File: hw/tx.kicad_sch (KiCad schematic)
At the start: 40 parts, among them T301 BN-43-202_DualPri_CTSec, U301 ICE40UP5K-SG48ITR, Y301 40MHz

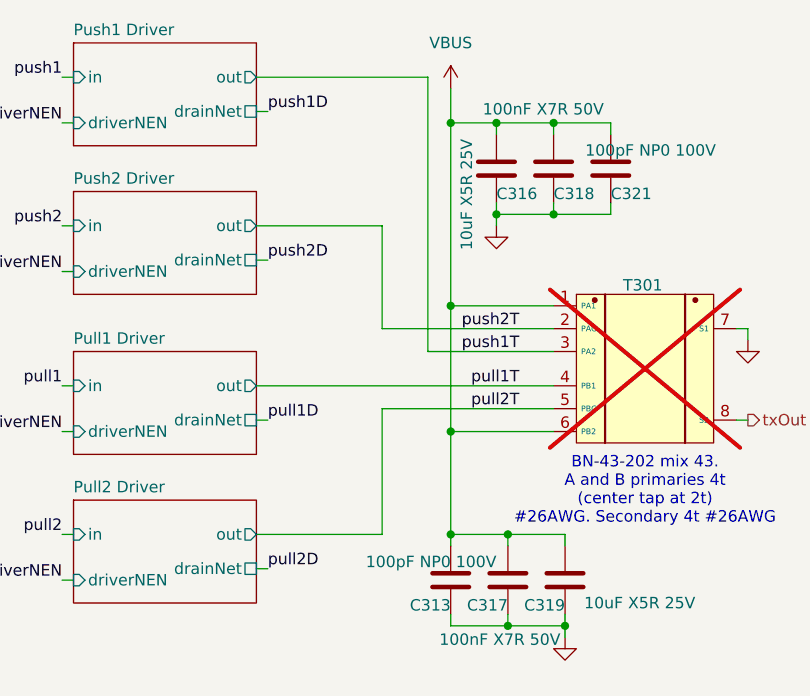
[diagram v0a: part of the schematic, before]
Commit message: Use relays and do layout over again to make these damned things fit
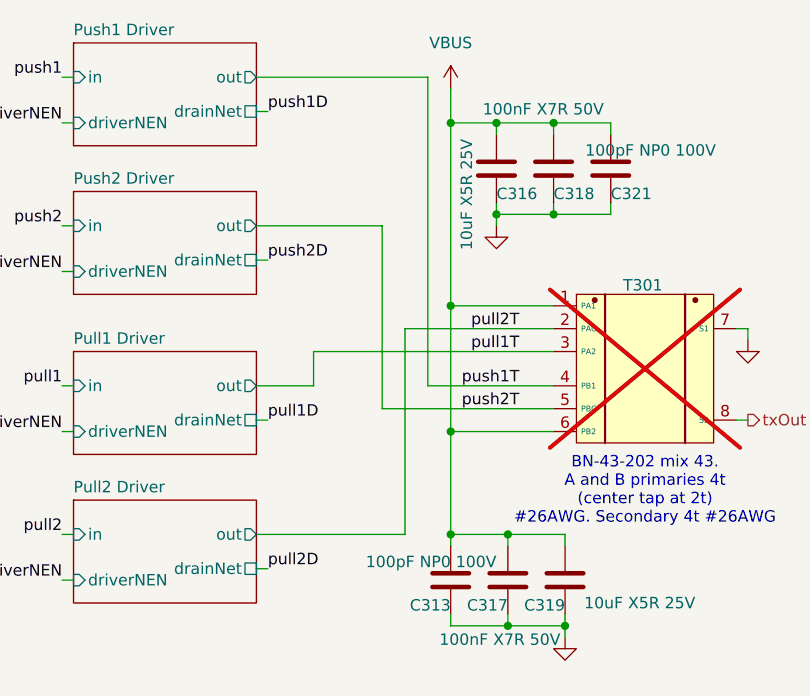
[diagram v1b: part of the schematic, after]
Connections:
- net pull1T: now also T301.3 (PA2); no longer T301.4 (PB1)
- net pull2T: now also T301.2 (PAC); no longer T301.5 (PBC)
- net push1T: now also T301.4 (PB1); no longer T301.3 (PA2)
- net push2T: now also T301.5 (PBC); no longer T301.2 (PAC)
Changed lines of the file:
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@@
-	(wire
-		(pts
-			(xy 218.44 35.56) (xy 218.44 46.99)
-		)
-		(stroke
-			(width 0)
-			(type default)
-		)
-	)
 	(wire
 		(pts
@@
 	(wire
 		(pts
-			(xy 218.44 69.85) (xy 218.44 55.88)
-		)
-		(stroke
-			(width 0)
-			(type default)
-		)
-	)
-	(wire
-		(pts
 			(xy 38.1 69.85) (xy 38.1 67.31)
 		)
@@
 	(wire
 		(pts
+			(xy 204.47 53.34) (xy 210.82 53.34)
+		)
+		(stroke
+			(width 0)
+			(type default)
+		)
+	)
+	(wire
+		(pts
 			(xy 229.87 132.08) (xy 232.41 132.08)
 		)
@@
 	(wire
 		(pts
+			(xy 218.44 55.88) (xy 237.49 55.88)
+		)
+		(stroke
+			(width 0)
+			(type default)
+		)
+	)
+	(wire
+		(pts
 			(xy 146.05 39.37) (xy 146.05 40.64)
 		)
@@
 	(wire
 		(pts
+			(xy 223.52 53.34) (xy 237.49 53.34)
+		)
+		(stroke
+			(width 0)
+			(type default)
+		)
+	)
+	(wire
+		(pts
+			(xy 220.98 46.99) (xy 220.98 69.85)
+		)
+		(stroke
+			(width 0)
+			(type default)
+		)
+	)
+	(wire
+		(pts
 			(xy 133.35 180.34) (xy 134.62 180.34)
 		)
@@
 	(wire
 		(pts
-			(xy 204.47 53.34) (xy 237.49 53.34)
-		)
-		(stroke
-			(width 0)
-			(type default)
-		)
-	)
-	(wire
-		(pts
 			(xy 113.03 102.87) (xy 113.03 101.6)
 		)
@@
 	(wire
 		(pts
+			(xy 210.82 53.34) (xy 210.82 49.53)
+		)
+		(stroke
+			(width 0)
+			(type default)
+		)
+	)
+	(wire
+		(pts
 			(xy 222.25 132.08) (xy 219.71 132.08)
 		)
@@
 	(wire
 		(pts
-			(xy 223.52 49.53) (xy 223.52 19.05)
+			(xy 223.52 19.05) (xy 223.52 53.34)
 		)
 		(stroke
@@
 	(wire
 		(pts
+			(xy 218.44 35.56) (xy 218.44 55.88)
+		)
+		(stroke
+			(width 0)
+			(type default)
+		)
+	)
+	(wire
+		(pts
 			(xy 184.15 133.35) (xy 184.15 128.27)
 		)
@@
 	(wire
 		(pts
-			(xy 204.47 69.85) (xy 218.44 69.85)
+			(xy 204.47 69.85) (xy 220.98 69.85)
 		)
 		(stroke
@@
 	(wire
 		(pts
+			(xy 220.98 46.99) (xy 237.49 46.99)
+		)
+		(stroke
+			(width 0)
+			(type default)
+		)
+	)
+	(wire
+		(pts
 			(xy 43.18 140.97) (xy 43.18 135.89)
 		)
@@
 	(wire
 		(pts
-			(xy 218.44 55.88) (xy 237.49 55.88)
-		)
-		(stroke
-			(width 0)
-			(type default)
-		)
-	)
-	(wire
-		(pts
 			(xy 106.68 102.87) (xy 106.68 101.6)
 		)
@@
 	(wire
 		(pts
+			(xy 210.82 49.53) (xy 237.49 49.53)
+		)
+		(stroke
+			(width 0)
+			(type default)
+		)
+	)
+	(wire
+		(pts
 			(xy 41.91 135.89) (xy 43.18 135.89)
 		)
@@
 	(wire
 		(pts
-			(xy 218.44 46.99) (xy 237.49 46.99)
-		)
-		(stroke
-			(width 0)
-			(type default)
-		)
-	)
-	(wire
-		(pts
 			(xy 160.02 58.42) (xy 160.02 59.69)
 		)
@@
 		(pts
 			(xy 248.92 133.35) (xy 251.46 133.35)
-		)
-		(stroke
-			(width 0)
-			(type default)
-		)
-	)
-	(wire
-		(pts
-			(xy 223.52 49.53) (xy 237.49 49.53)
 		)
 		(stroke
@@
 	)
 	(label "pull2T"
-		(at 233.68 55.88 180)
+		(at 233.68 46.99 180)
 		(effects
 			(font
@@
 	)
 	(label "push2T"
-		(at 233.68 46.99 180)
+		(at 233.68 55.88 180)
 		(effects
 			(font
@@
 	)
 	(label "pull1T"
+		(at 233.68 49.53 180)
+		(effects
+			(font
+				(size 1.27 1.27)
+			)
+			(justify right bottom)
+		)
+	)
+	(label "push1T"
 		(at 233.68 53.34 180)
 		(effects
 			(font
-				(size 1.27 1.27)
-			)
-			(justify right bottom)
-		)
-	)
-	(label "push1T"
-		(at 233.68 49.53 180)
-		(effects
-			(font
